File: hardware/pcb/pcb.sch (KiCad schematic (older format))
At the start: 15 parts, among them Q1 FDN339AN, SW1 SW_SPST, U1 WeMos_D1_mini, U2 TSOP38236

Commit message: Added schematic
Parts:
- added BT1: protected 18650, Battery:BatteryHolder_Keystone_1042_1x18650, symbol Device:Battery_Cell
- added C2, C5, C6: 4.7uF, Capacitor_SMD:C_0805_2012Metric_Pad1.15x1.40mm_HandSolder, symbol Device:C_Small
- added C3, C4: 10nF, Capacitor_SMD:C_0603_1608Metric_Pad1.05x0.95mm_HandSolder, symbol Device:C_Small
- added D4: MBRA140, Diode_SMD:D_SMA, symbol Device:D_Schottky_Small
- added D5: charging, LED_SMD:LED_0603_1608Metric_Pad1.05x0.95mm_HandSolder, symbol Device:LED_Small
- added D6: charged, LED_SMD:LED_0603_1608Metric_Pad1.05x0.95mm_HandSolder, symbol Device:LED_Small
- added J1: TYPE-C-31-M-12, Connector_USB:USB_C_Receptacle_HRO_TYPE-C-31-M-12, symbol Connector:USB_C_Receptacle_USB2.0
- added R10, R14, R15: 10k, Resistor_SMD:R_0603_1608Metric_Pad1.05x0.95mm_HandSolder, symbol Device:R_Small
- added R11, R12: 470R, Resistor_SMD:R_0603_1608Metric_Pad1.05x0.95mm_HandSolder, symbol Device:R_Small
- added R13: 10mR, Resistor_SMD:R_0603_1608Metric_Pad1.05x0.95mm_HandSolder, symbol Device:R_Small
- added R8, R9: 5k1, Resistor_SMD:R_0603_1608Metric_Pad1.05x0.95mm_HandSolder, symbol Device:R_Small
- added U3: MCP73831-2-OT, Package_TO_SOT_SMD:SOT-23-5, symbol Battery_Management:MCP73831-2-OT
- added U4: BQ27441DRZR-G1A, Package_SON:Texas_S-PDSO-N12, symbol Battery_Management:BQ27441DRZR-G1A
- added U5: TLV75733PDBV, Package_TO_SOT_SMD:SOT-23-5, symbol Regulator_Linear:TLV75733PDBV
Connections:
- net IR_DeMod_SIG is gone; now on net IR_SIGNAL: U1.11 (D4)
- net +3V3: now also C6.2, R15.2, U5.5 (OUT)
- net GND: now also BT1.2 (-), C2.1, C3.1, C4.1, C5.2, C6.1, J1.A1 (GND), J1.A12 (GND), J1.B1 (GND), J1.B12 (GND), J1.S1 (SHIELD), R10.1, R12.2, R14.1, R8.2, R9.1, U3.2 (VSS), U4.13 (PAD), U4.3 (VSS), U5.2 (GND)
- net IR_BLASTER: no longer U1.4 (SCK/D5)
- net IR_DEMOD_SIG renamed IR_SIGNAL
- net IR_DeMod_VCC renamed IR_RECV_VCC
- net Power management/SCL renamed SCL
- net SCL: now also U4.2 (SCL)
- net Power management/SDA renamed SDA
- net SDA: now also U4.1 (SDA)
- net Power management/~LOW_BAT renamed ~LOW_BAT
- net ~LOW_BAT: now also R15.1, U4.12 (GPOUT)
- net factory_reset renamed factory_rst
- new net: J1.A5 (CC1), R8.1
- new net: J1.B5 (CC2), R9.2
- new net: R14.2, U4.10 (BIN)
- new net: D5.2 (A), R11.2
- new net: D5.1 (K), D6.2 (A), U3.1 (STAT)
- new net: D6.1 (K), R12.1
- new net: D4.1 (K), U3.4 (VDD)
- new net: R10.2, U3.5 (PROG)
- new net +1V8: C4.2, U4.5 (VDD)
- new net +BATT: BT1.1 (+), C3.2, R13.1, U4.6 (BAT), U4.8 (SRP)
- new net IR_BLAST: U1.4 (SCK/D5)
- new net VBUS: D4.2 (A), J1.A4 (VBUS), J1.A9 (VBUS), J1.B4 (VBUS), J1.B9 (VBUS), R11.1
- new net VCCQ: C2.2, C5.1, R13.2, U3.3 (VBAT), U4.7 (SRN), U5.1 (IN), U5.3 (EN)
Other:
- note added: "3V3 LDO"
- note added: "Charging"
- note added: "Fuel gauge"
- note added: "Logic"
- note added: "Power"
- moved on the sheet: C1, D1, D2, D3, Q1, R1, R2, R3, R4, R5, R6, R7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

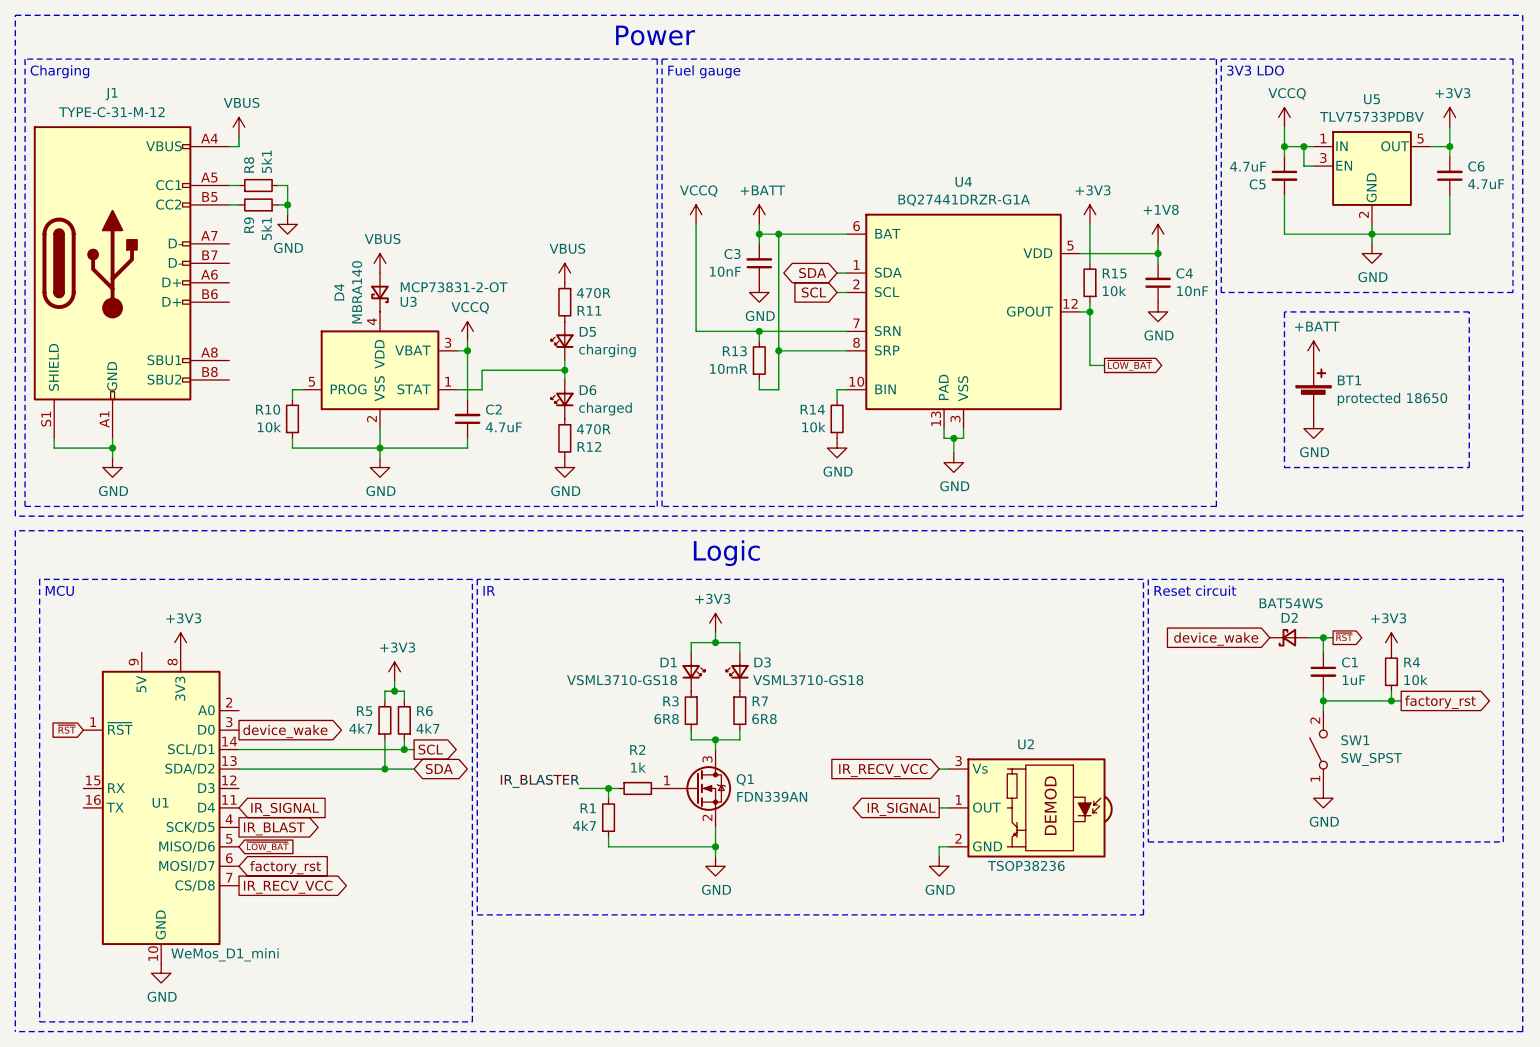
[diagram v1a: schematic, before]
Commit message: Centered USB-C, Added cutouts for 15mm case posts
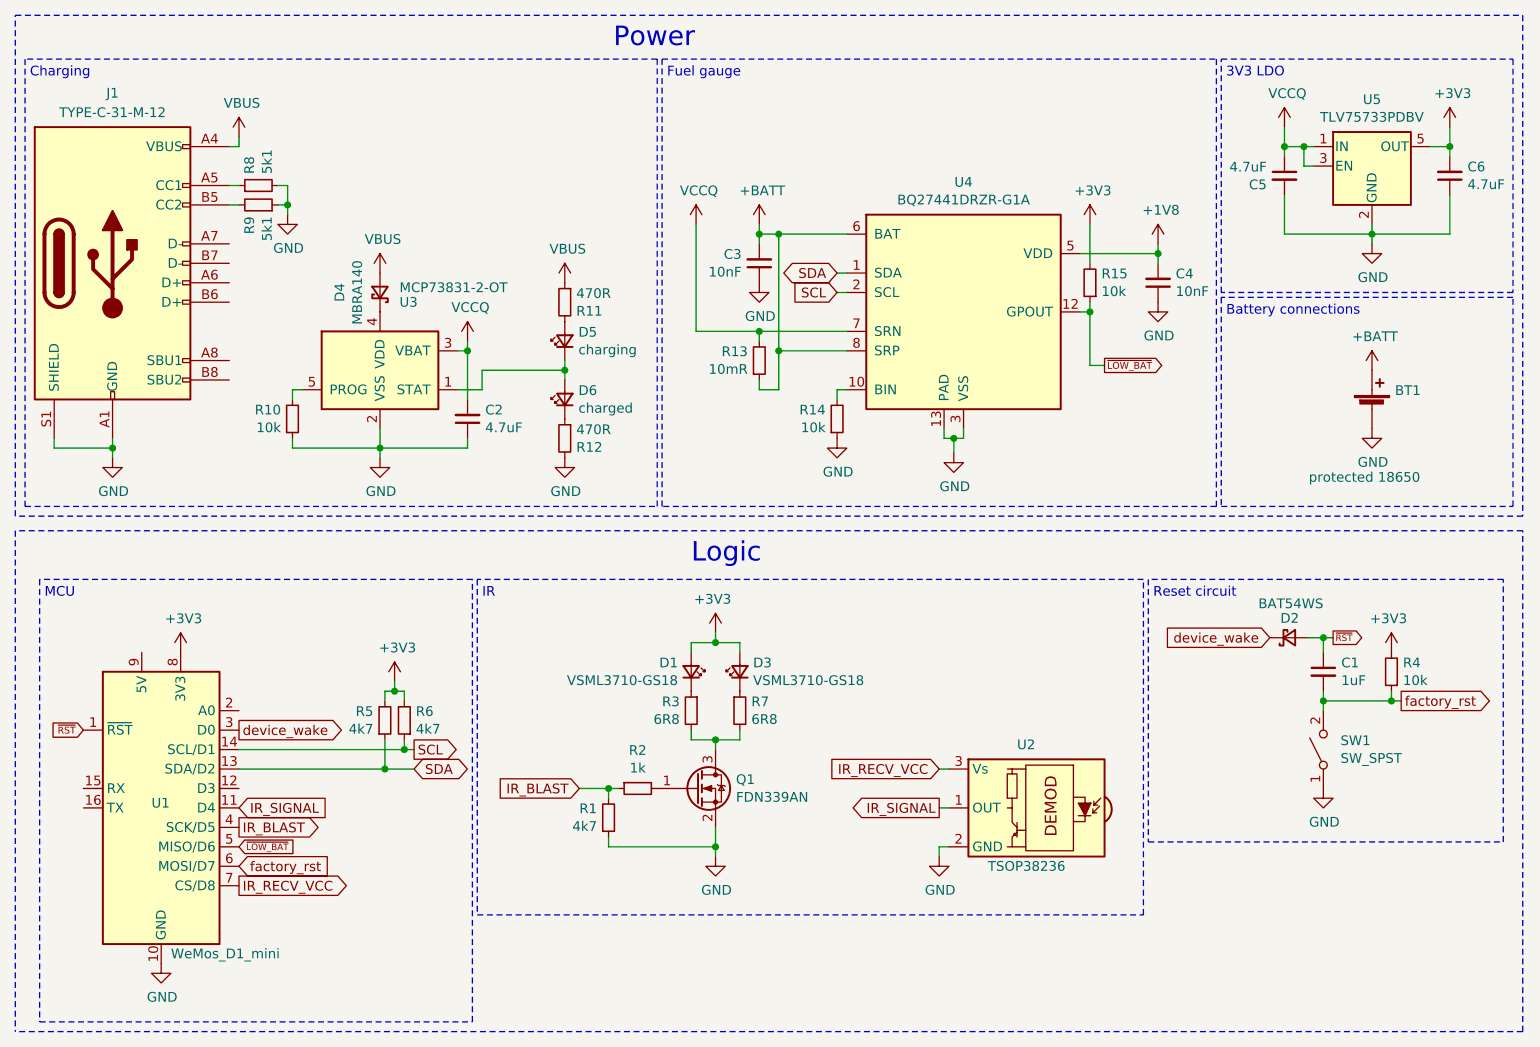
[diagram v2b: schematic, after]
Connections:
- net IR_BLASTER is gone; now on net IR_BLAST: R1.2, R2.1
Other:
- note added: "Battery connections"
- moved on the sheet: BT1
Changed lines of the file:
@@
 L power:GND #PWR?
 U 1 1 5E88BDD0
-P 8625 3075
+P 8925 3125
 AR Path="/5E707A75/5E88BDD0" Ref="#PWR?"  Part="1"
 AR Path="/5E88BDD0" Ref="#PWR02"  Part="1"
-F 0 "#PWR02" H 8625 2825 50  0001 C CNN
-F 1 "GND" H 8630 2902 50  0000 C CNN
-F 2 "" H 8625 3075 50  0001 C CNN
-F 3 "" H 8625 3075 50  0001 C CNN
-	1    8625 3075
+F 0 "#PWR02" H 8925 2875 50  0001 C CNN
+F 1 "GND" H 8930 2952 50  0000 C CNN
+F 2 "" H 8925 3125 50  0001 C CNN
+F 3 "" H 8925 3125 50  0001 C CNN
+	1    8925 3125
 	1    0    0    -1
 $EndComp
@@
 $EndComp
 Wire Notes Line
-	8475 3325 9425 3325
-Wire Notes Line
-	8475 2525 8475 3325
-Wire Notes Line
-	9425 2525 8475 2525
-Wire Notes Line
-	9425 3325 9425 2525
+	8150 3525 9650 3525
+Wire Notes Line
+	8150 2450 8150 3525
+Wire Notes Line
+	9650 2450 8150 2450
+Wire Notes Line
+	9650 3525 9650 2450
 Text Notes 5300 1325 0    50   ~ 0
 Fuel gauge
@@
 L power:+BATT #PWR?
 U 1 1 5E88BC77
-P 8625 2775
+P 8925 2825
 AR Path="/5E707A75/5E88BC77" Ref="#PWR?"  Part="1"
 AR Path="/5E88BC77" Ref="#PWR01"  Part="1"
-F 0 "#PWR01" H 8625 2625 50  0001 C CNN
-F 1 "+BATT" H 8640 2948 50  0000 C CNN
-F 2 "" H 8625 2775 50  0001 C CNN
-F 3 "" H 8625 2775 50  0001 C CNN
-	1    8625 2775
+F 0 "#PWR01" H 8925 2675 50  0001 C CNN
+F 1 "+BATT" H 8940 2998 50  0000 C CNN
+F 2 "" H 8925 2825 50  0001 C CNN
+F 3 "" H 8925 2825 50  0001 C CNN
+	1    8925 2825
 	1    0    0    -1
 $EndComp
@@
 L Device:Battery_Cell BT?
 U 1 1 5E88BC71
-P 8625 2975
+P 8925 3025
 AR Path="/5E707A75/5E88BC71" Ref="BT?"  Part="1"
 AR Path="/5E88BC71" Ref="BT1"  Part="1"
-F 0 "BT1" H 8743 3071 50  0000 L CNN
-F 1 "protected 18650" H 8743 2980 50  0000 L CNN
-F 2 "Battery:BatteryHolder_Keystone_1042_1x18650" V 8625 3035 50  0001 C CNN
-F 3 "~" V 8625 3035 50  0001 C CNN
-	1    8625 2975
+F 0 "BT1" H 9043 3121 50  0000 L CNN
+F 1 "protected 18650" H 8600 2675 50  0000 L CNN
+F 2 "Battery:BatteryHolder_Keystone_1042_1x18650" V 8925 3085 50  0001 C CNN
+F 3 "~" V 8925 3085 50  0001 C CNN
+	1    8925 3025
 	1    0    0    -1
 $EndComp
@@
 	0    -1   -1   0
 $EndComp
-Text Label 4850 4975 2    50   ~ 0
-IR_BLASTER
 Connection ~ 5000 4975
 Wire Wire Line
@@
 P 7475 2075
 AR Path="/5E707A75/5EB65D23" Ref="#PWR?"  Part="1"
-AR Path="/5EB65D23" Ref="#PWR?"  Part="1"
-F 0 "#PWR?" H 7475 1925 50  0001 C CNN
+AR Path="/5EB65D23" Ref="#PWR0109"  Part="1"
+F 0 "#PWR0109" H 7475 1925 50  0001 C CNN
 F 1 "+3V3" H 7490 2248 50  0000 C CNN
 F 2 "" H 7475 2075 50  0001 C CNN
@@
 	7475 2525 7475 2800
 Connection ~ 7475 2525
+Text GLabel 4850 4975 0    50   Input ~ 0
+IR_BLAST
+Text Notes 8175 2550 0    50   ~ 0
+Battery connections
 $EndSCHEMATC
